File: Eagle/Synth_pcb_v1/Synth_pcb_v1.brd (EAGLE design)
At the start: 118 x 68 mm, 76 parts, among them IC3 LM358N, IC4 LM358N, IC5 LM358N, IC6 LM358N, T1 BC547, T2 BC547, T3 BC547, T4 BC547, T5 BC547, T6 BC547, X1 MAB5SH

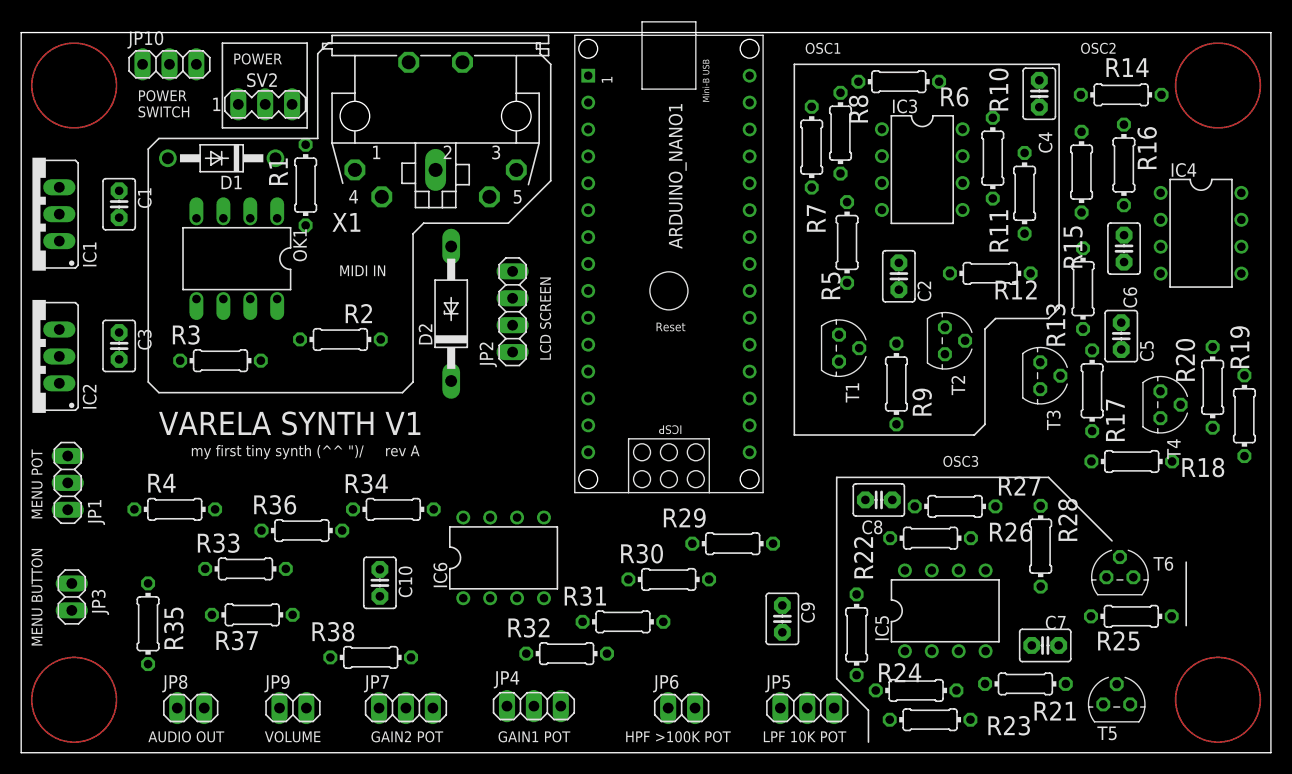
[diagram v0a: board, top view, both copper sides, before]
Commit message: Most of the PCB is routed. Revision is needed
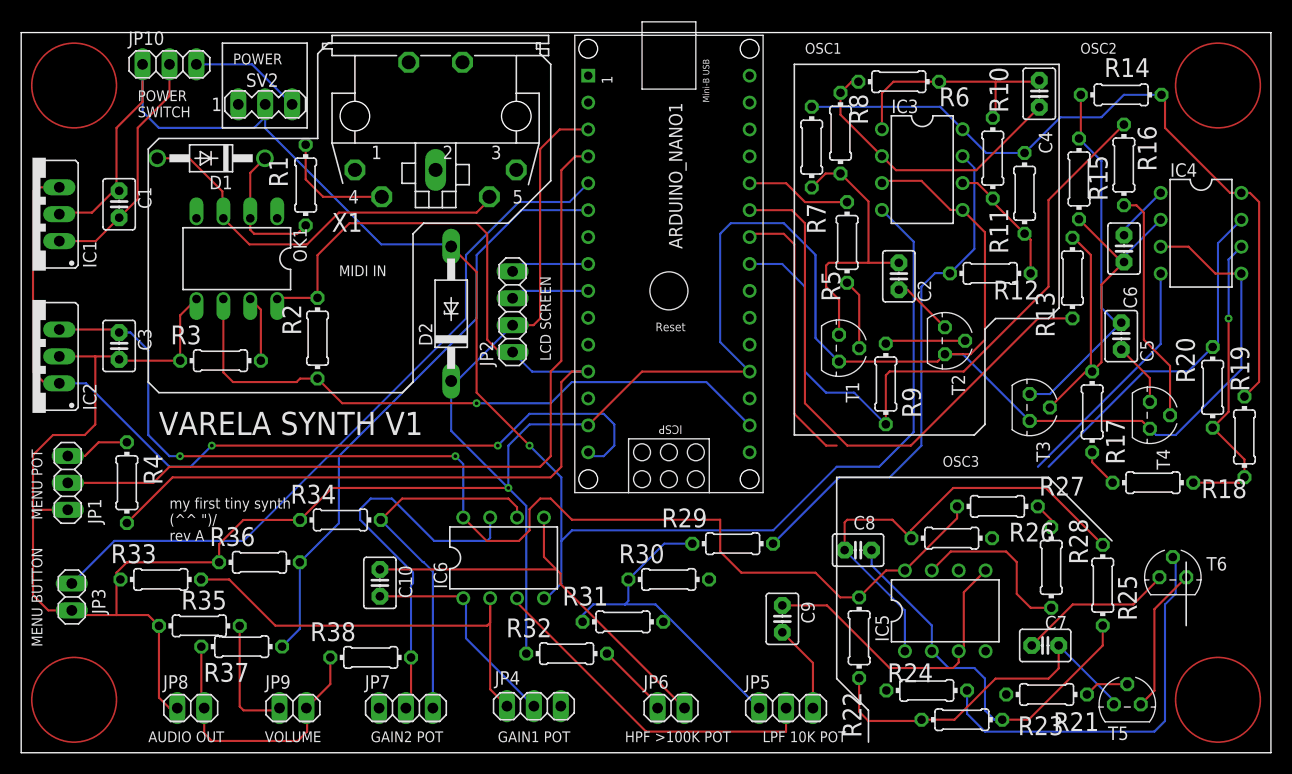
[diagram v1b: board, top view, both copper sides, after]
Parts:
- moved R33 8.06 mm to (13.2, 16.4)
- moved R4 5.18 mm to (9.98, 25.5), turned to 90 degrees
- moved C8 5.13 mm to (79.0, 19.1), turned to 180 degrees
- moved R34 5.10 mm to (30.1, 22.0)
- moved R36 5.00 mm to (22.5, 18.0)
- moved T6 5.00 mm to (108.7, 16.6)
- moved R35 4.84 mm to (16.8, 12.0), turned to 0 degrees
- moved R27 4.00 mm to (92.2, 23.3)
- moved R25 3.99 mm to (102.1, 15.8), turned to 270 degrees
- moved R37 3.16 mm to (20.8, 10.0)
- moved T3 3.16 mm to (95.2, 32.6)
- moved R23 3.00 mm to (88.8, 3.12)
- moved R18 2.83 mm to (106.9, 25.5)
- moved R21 2.24 mm to (96.8, 5.50)
- moved R28 2.24 mm to (97.3, 17.5)
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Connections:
- net CONTROL_OSC1: now also ARDUINO_NANO1.26; no longer ARDUINO_NANO1.24
- net CONTROL_OSC3: now also ARDUINO_NANO1.24; no longer ARDUINO_NANO1.26
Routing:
- net GND: track 0.00 -> 373.2 mm, vias 0 -> 1
- net REG_5V: track 0.00 -> 184.4 mm, vias 0 -> 2
- net 0V_IN: track 0.00 -> 183.3 mm, vias 0 -> 1
- net 5V: track 0.00 -> 100.6 mm
- net V+: track 0.00 -> 85.8 mm, vias 0 -> 2
- net IN_0: track 0.00 -> 77.1 mm
- net IN_1: track 0.00 -> 67.9 mm
- net TRIGGER_TRI: track 0.00 -> 65.5 mm
- net MIDI_IN: track 0.00 -> 60.6 mm, vias 0 -> 1
- net AUDIO_IN: track 0.00 -> 56.9 mm
- net CONTROL_OSC2: track 0.00 -> 54.6 mm
- net OUT_OSC1: track 0.00 -> 48.6 mm
- net N$45: track 0.00 -> 44.4 mm
- net N$58: track 0.00 -> 42.4 mm
- net HPF_OUT: track 0.00 -> 40.2 mm
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
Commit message: PCB routing complete, ready for revision.
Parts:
- C10: value 10nF -> 220nF
- C2: value 22uF -> 220uF
- C3: value 220uF -> 22uF
- C4: value 220nF -> 22uF
- C5: value 22uF -> 220nF
- C7: value 22uF -> 100nF
- C8: value 220nF -> 10nF
- C9: value 100nF -> 22uF
- D1: value 1N4004 -> ZY; device diode:DO41-10 -> diode:P1Z12
- D2: value ZY -> 1N4004; device diode:P1Z12 -> diode:DO41-10
- JP2: device pinhead:1X04 -> pinhead:1X02
- JP3: device pinhead:1X02 -> pinhead:1X04
- JP5, JP7: device pinhead:1X03 -> pinhead:1X02
- JP8, JP9: device pinhead:1X02 -> pinhead:1X03
- R11: value 4.7k -> 1k
- R12, R18, R26, R34, R7, R8: value 1k -> 10k
- R16, R17, R3, R30, R32, R36, R6: value 10k -> 1k
- R19, R27: value 4.7k -> 10k
- R2: value 470 -> NC
- R20: value 1k -> 4.7k
- R21: value 10k -> 4.7k
- R35: value NC -> 4.7k
- R4: value 1k -> 470
- moved C3 94.6 mm to (103.9, 39.3)
- moved R6 81.8 mm to (20.8, 10.0)
- moved R35 76.1 mm to (92.2, 22.3), turned to 180 degrees
- moved R34 74.4 mm to (104.1, 13.8), turned to 270 degrees
- moved C2 73.9 mm to (9.25, 38.4)
- moved JP10 69.7 mm to (48.4, 4.40), turned to 180 degrees
- moved R7 65.2 mm to (22.5, 18.0), turned to 0 degrees
- moved R36 64.4 mm to (86.9, 20.3), turned to 180 degrees
- moved R5 60.2 mm to (18.8, 37.0), turned to 0 degrees
- moved JP6 57.5 mm to (4.78, 14.7), turned to 90 degrees
- moved JP8 56.2 mm to (72.2, 4.22)
- moved R23 53.1 mm to (91.7, 56.1), turned to 90 degrees
- moved JP3 49.6 mm to (46.4, 41.6)
- moved JP4 48.8 mm to (4.40, 25.5), turned to 90 degrees
- moved R32 48.3 mm to (99.3, 16.5), turned to 90 degrees
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- renumbered SV2 to SV1
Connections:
- removed net N$21 (its old number): R5.1, T1.2
- new net N$22: R13.1, T4.2
- net 0V_IN: now also D1.A, JP1.1; no longer D2.A, JP10.1
- net 12V_IN: now also JP1.2; no longer JP10.2
- net 5V: now also JP3.1, R3.1, R4.2; no longer JP2.1, R2.2, R4.1
- net AMP1_OUT: now also C8.2, JP10.2; no longer C10.2, JP4.2
- net AMP2_OUT: now also JP2.2, JP5.2, R33.1, R6.2; no longer JP8.2, JP9.2, R37.2, R38.1
- net AUDIO_IN: now also R6.1, R7.2; no longer R36.2, R37.1
- net CONTROL_OSC1: now also R9.2; no longer R5.2
- net CONTROL_OSC2: now also R8.2; no longer R13.2
- net CONTROL_OSC3: now also R24.2; no longer R21.2
- net GND: now also C2.2, C7.1, D1.C, JP2.1, JP3.2, JP4.1, JP6.1, R2.1, R31.1, R37.1, R38.1, R5.1, R7.1; no longer C3.2, C9.1, D2.C, JP1.1, JP2.2, JP3.1, JP8.1, R3.1, R32.1, R33.1, R34.1, R35.1, R36.1
- net GND2: now also JP7.1, R31.2; no longer JP6.1, R32.2
- net HPF_OUT: now also C8.1, JP7.2; no longer C10.1, JP6.2
- net IN_0: now also JP4.2; no longer JP1.2
- net IN_1: now also JP6.2; no longer JP3.2
- net LPF_OUT: now also JP8.2; no longer JP5.2
- net MIDI_IN: now also R4.1; no longer R2.1
- net N$1: now also D2.A; no longer D1.A
- net N$11: now also C4.2, T4.3; no longer C2.2, T2.3
- net N$13: now also JP4.3, R3.2; no longer JP1.3, R4.2
- net N$16: now also C6.1, IC4.2, R14.2, R19.2; no longer C4.1, IC3.2, R6.2, R8.2
- net N$2: now also JP9.2, R33.2; no longer JP7.2, R38.2
- net N$24: now also C4.1, R11.2, R14.1, T2.3; no longer C2.1, R7.2, R8.1, T1.3
- net N$25: now also C6.2, IC4.1, R19.1, R23.2; no longer C4.2, IC3.1, R10.2, R6.1
- net N$26: now also IC4.6, R17.2, R21.1, R23.1; no longer IC3.6, R10.1, R11.1, R12.2
- net N$29: now also C3.1, R10.2, T1.3; no longer C5.1, R14.2, T3.3
- net N$30: now also C3.2, T3.3; no longer C5.2, T4.3
- net N$33: now also C5.1, IC3.2, R18.2; no longer C6.1, IC4.2, R17.2
- net N$34: now also C5.2, IC3.1, R18.1, R22.2; no longer C6.2, IC4.1, R17.1, R18.2
- net N$35: now also IC3.6, R16.2, R20.1, R22.1; no longer IC4.6, R18.1, R19.1, R20.2
- net N$36: now also R8.1, T1.2; no longer R13.1, T3.2
- net N$37: now also R12.1, T3.2; no longer R16.1, T4.2
- net N$40: now also C9.1, R28.2, R30.1; no longer C7.1, R22.2, R23.1
- net N$41: now also C9.2; no longer C7.2
- net N$44: now also C10.1, R30.2, R34.2; no longer C8.1, R23.2, R25.2
- net N$45: now also C10.2, R34.1, R36.2; no longer C8.2, R25.1, R26.2
- net N$46: now also R32.2, R35.1, R36.1; no longer R26.1, R27.1, R28.2
- net N$47: now also R24.1; no longer R21.1
- net N$48: now also R29.1; no longer R24.1
- net N$5: now also D2.C; no longer D1.C
- net N$57: now also JP9.3, R38.2; no longer JP7.3, R34.2
- net N$58: now also JP10.3, R37.2; no longer JP4.3, R33.2
- net N$59: now also C7.2, JP8.3; no longer C9.2, JP5.3
- net N$63: now also JP5.1, R2.2; no longer JP9.1, R35.2
- net N$7: now also R5.2; no longer R3.2
- net OUT_OSC1: now also IC4.7, R17.1, R27.2; no longer IC3.7, R12.1, R29.2
- net OUT_OSC2: now also IC3.7, R16.1, R26.2; no longer IC4.7, R20.1, R30.2
- net OUT_OSC3: now also R25.2, R32.1; no longer R28.1, R31.2
- net OUT_WAV: now also JP8.1, R25.1, R26.1, R27.1; no longer JP5.1, R29.1, R30.1, R31.1
- net PWR: now also JP1.3; no longer JP10.3
- net REG_5V: now also C2.1, R10.1, R11.1, R20.2, R21.2, R28.1, R35.2; no longer C3.1, R11.2, R14.1, R19.2, R22.1, R27.2, R7.1
- net SCL: now also JP3.3; no longer JP2.3
- net SDA: now also JP3.4; no longer JP2.4
- net TRIGGER_TRI: now also R12.2, R13.2, R29.2; no longer R16.2, R24.2, R9.2
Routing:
- net TRIGGER_TRI: track 65.5 -> 115.0 mm, vias 0 -> 1
- net CONTROL_OSC3: track 26.0 -> 67.2 mm, vias 0 -> 1
- net OUT_OSC2: track 33.3 -> 71.4 mm, vias 0 -> 2
- net N$34: track 9.09 -> 44.7 mm, vias 0 -> 2
- net REG_5V: track 184.4 -> 219.8 mm, vias 2 -> 3
- net 0V_IN: track 183.3 -> 216.4 mm, vias 1 -> 3
- net GND: track 373.2 -> 404.9 mm
- net OUT_OSC3: track 16.0 -> 44.6 mm
- net N$46: track 2.48 -> 22.5 mm
- net OUT_WAV: track 31.7 -> 21.3 mm
- net OUT_OSC1: track 48.6 -> 58.4 mm
- net N$22: track 0.00 -> 7.60 mm
- net N$21 (its old number): track 6.64 -> 0.00 mm
- net N$16: track 27.6 -> 30.2 mm
- net N$40: track 34.3 -> 31.9 mm
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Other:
- outline, holes or cut-outs redrawn
